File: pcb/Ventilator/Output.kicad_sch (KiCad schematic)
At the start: 16 parts, among them J3 Screw_Terminal_01x08, K1 FINDER-40.52.7.012.0000, K2 FINDER-40.52.7.012.0000, K3 FINDER-40.52.7.012.0000, Q1 NUD3160, Q2 NUD3160, Q3 NUD3160

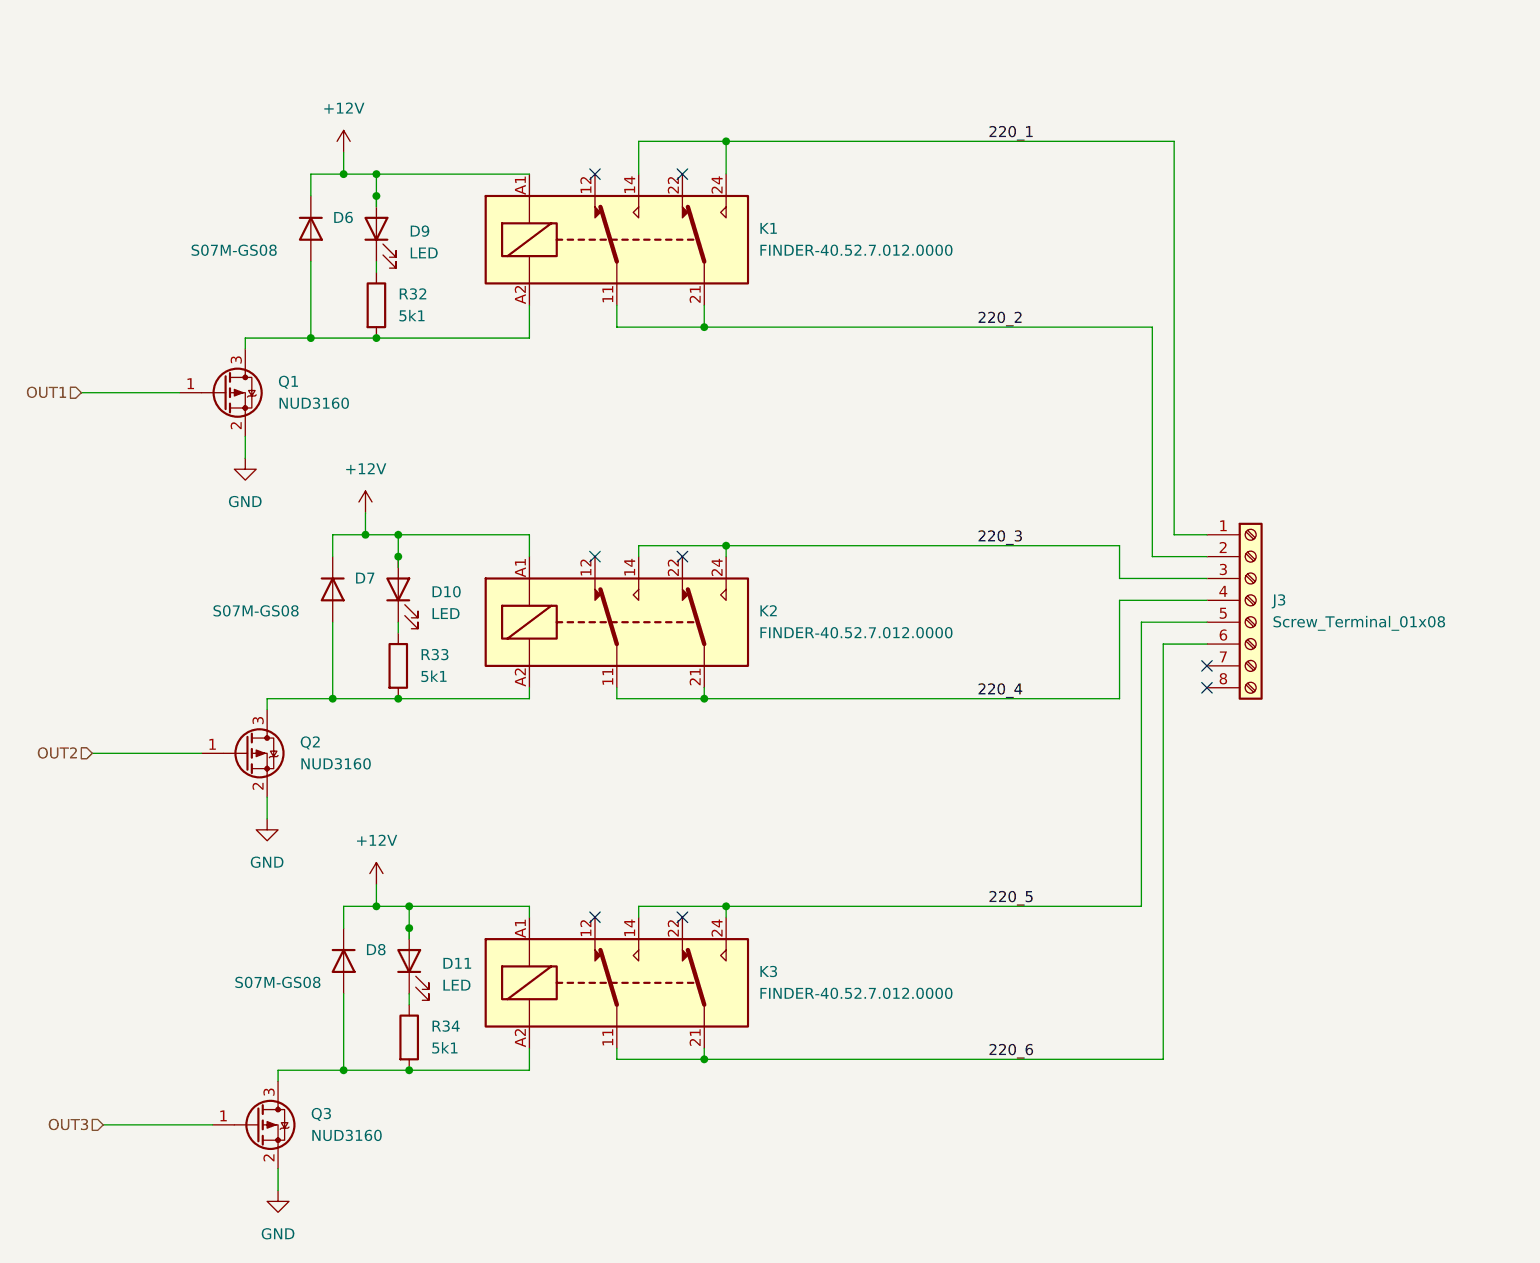
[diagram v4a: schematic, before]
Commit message: -Ventcontrol 1.2 (routed)
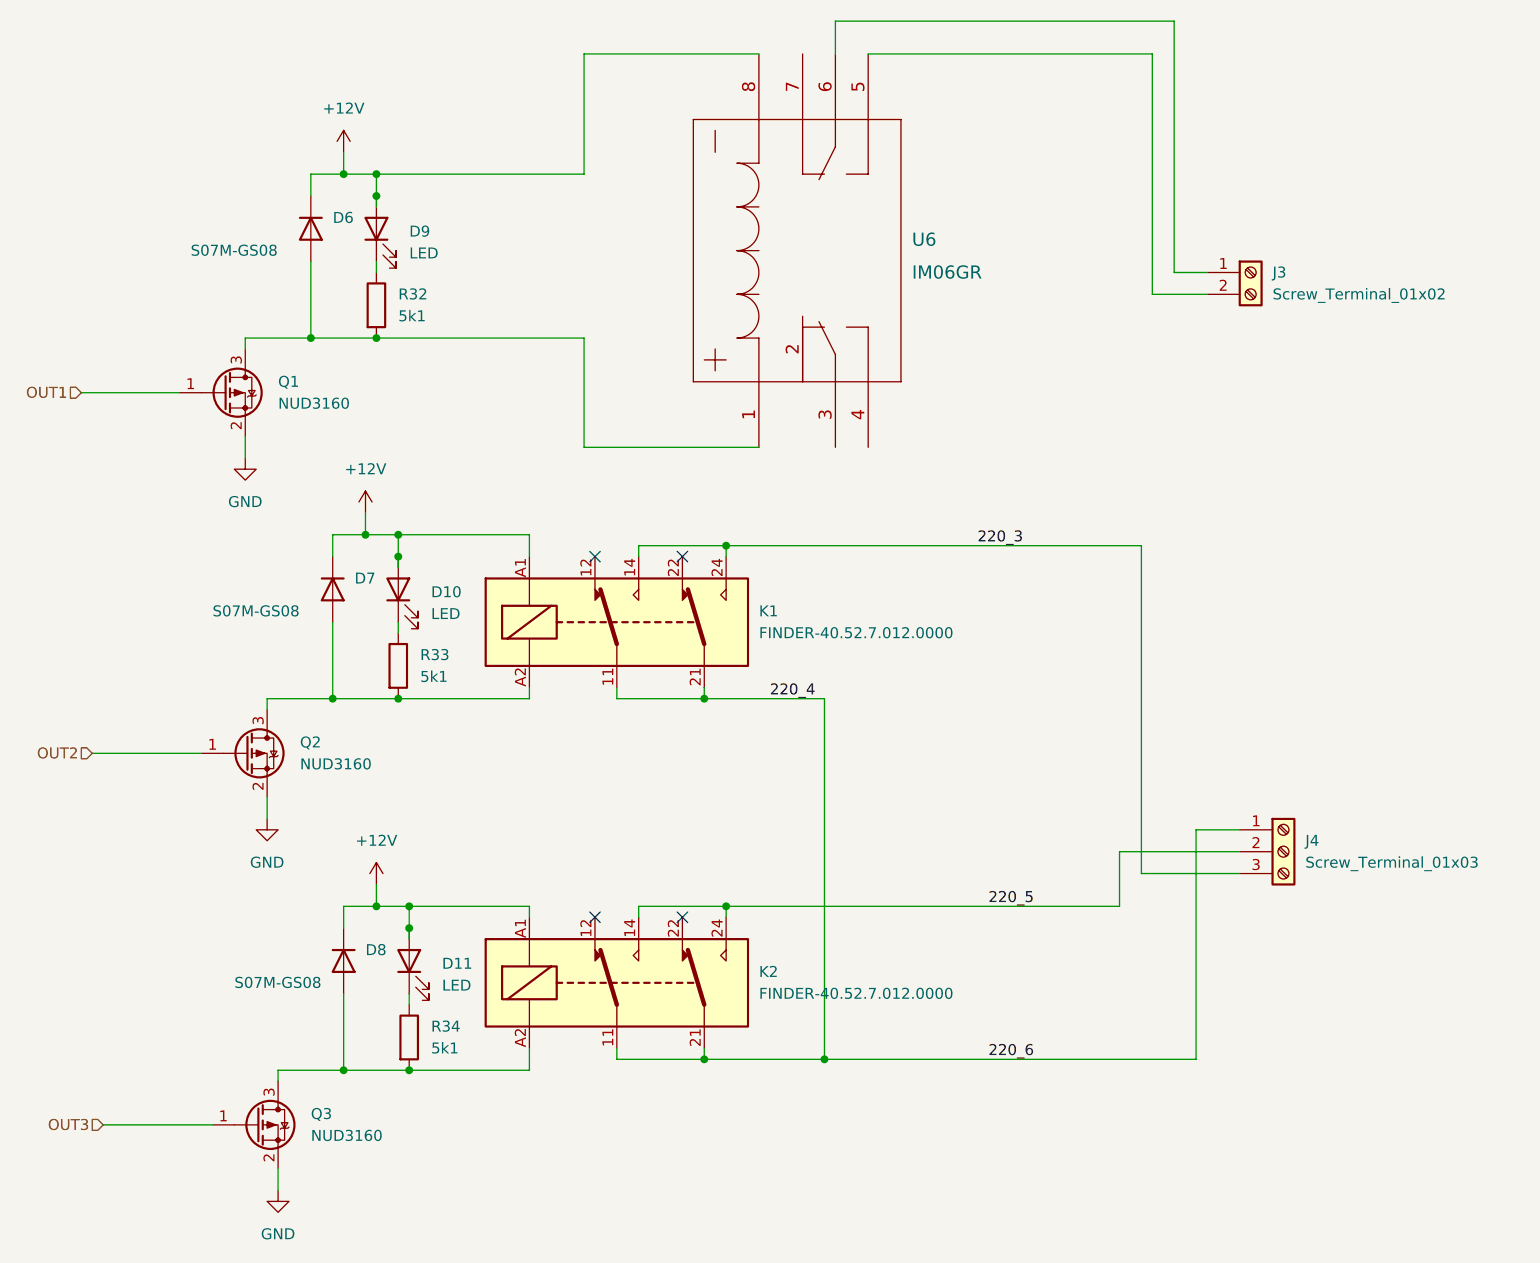
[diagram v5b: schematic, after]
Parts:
- removed J3: Screw_Terminal_01x08, TerminalBlock_Phoenix:TerminalBlock_Phoenix_MKDS-1,5-8_1x08_P5.00mm_Horizontal, symbol Connector:Screw_Terminal_01x08
- removed K1: FINDER-40.52.7.012.0000, Relay_THT:Relay_DPDT_Finder_40.52, symbol Relay:FINDER-40.52
- added J3: Screw_Terminal_01x02, TerminalBlock_Phoenix:TerminalBlock_Phoenix_MKDS-1,5-2-5.08_1x02_P5.08mm_Horizontal, symbol Connector:Screw_Terminal_01x02
- added J4: Screw_Terminal_01x03, TerminalBlock_Phoenix:TerminalBlock_Phoenix_MKDS-1,5-3-5.08_1x03_P5.08mm_Horizontal, symbol Connector:Screw_Terminal_01x03
- added U6: IM06GR, IM06GR:IM06GR, symbol 2023-01-29_17-38-59:IM06GR
- renumbered K2 to K1, K3 to K2
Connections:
- net 220_6 is gone; now on net 220_4: K2.11, K2.21
- net +12V: now also U6.8
- net 220_3: now also J4.3 (Pin_3)
- net 220_4: now also J4.1 (Pin_1)
- net 220_5: now also J4.2 (Pin_2)
- net at D6.2 (A), Q1.3 (D), R32.2: now also U6.1
- new net: J3.2 (Pin_2), U6.5
- new net: J3.1 (Pin_1), U6.6
- no-connect marks 8 -> 4

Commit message: - last changes
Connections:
- no-connect marks 4 -> 8
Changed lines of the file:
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@@
   )
   (no_connect (at 146.05 85.09))
+  (no_connect (at 160.02 57.15))
   (no_connect (at 146.05 127))
   (no_connect (at 135.89 85.09))
+  (no_connect (at 160.02 26.67))
+  (no_connect (at 163.83 72.39))
+  (no_connect (at 167.64 72.39))
   (no_connect (at 135.89 127))
   (wire (pts (xy 163.83 22.86) (xy 203.2 22.86))

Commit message: - as ordered
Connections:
- net +12V: now also U6.1; no longer U6.8
- net at D6.2 (A), Q1.3 (D), R32.2: now also U6.8; no longer U6.1
- net at U6.3: now also J3.1 (Pin_1), U6.6
- net at U6.4: now also J3.2 (Pin_2), U6.5
- no-connect marks 8 -> 5
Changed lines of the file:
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@@
   (junction (at 151.13 125.73) (diameter 0) (color 0 0 0 0)
   )
+  (junction (at 189.23 22.86) (diameter 0) (color 0 0 0 0)
+  )
   (junction (at 114.3 128.27) (diameter 0) (color 0 0 0 0)
   )
@@
   (junction (at 148.59 143.51) (diameter 0) (color 0 0 0 0)
   )
+  (junction (at 184.15 26.67) (diameter 0) (color 0 0 0 0)
+  )
   (junction (at 113.03 82.55) (diameter 0) (color 0 0 0 0)
   )
@@
   )
   (no_connect (at 146.05 85.09))
-  (no_connect (at 160.02 57.15))
   (no_connect (at 146.05 127))
   (no_connect (at 135.89 85.09))
-  (no_connect (at 160.02 26.67))
-  (no_connect (at 163.83 72.39))
-  (no_connect (at 167.64 72.39))
+  (no_connect (at 160.02 72.39))
   (no_connect (at 135.89 127))
-  (wire (pts (xy 163.83 22.86) (xy 203.2 22.86))
+  (wire (pts (xy 163.83 22.86) (xy 189.23 22.86))
     (stroke (width 0) (type default) (color 0 0 0 0))
   )
@@
     (stroke (width 0) (type default) (color 0 0 0 0))
   )
+  (wire (pts (xy 189.23 22.86) (xy 203.2 22.86))
+    (stroke (width 0) (type default) (color 0 0 0 0))
+  )
   (wire (pts (xy 199.39 121.92) (xy 210.82 121.92))
     (stroke (width 0) (type default) (color 0 0 0 0))
   )
-  (wire (pts (xy 134.62 26.67) (xy 154.94 26.67))
-    (stroke (width 0) (type default) (color 0 0 0 0))
-  )
   (wire (pts (xy 128.27 144.78) (xy 128.27 142.24))
     (stroke (width 0) (type default) (color 0 0 0 0))
   )
-  (wire (pts (xy 110.49 59.69) (xy 134.62 59.69))
+  (wire (pts (xy 110.49 59.69) (xy 137.16 59.69))
     (stroke (width 0) (type default) (color 0 0 0 0))
   )
@@
     (stroke (width 0) (type default) (color 0 0 0 0))
   )
-  (wire (pts (xy 110.49 40.64) (xy 134.62 40.64))
+  (wire (pts (xy 110.49 40.64) (xy 138.43 40.64))
     (stroke (width 0) (type default) (color 0 0 0 0))
   )
@@
     (stroke (width 0) (type default) (color 0 0 0 0))
   )
-  (wire (pts (xy 134.62 72.39) (xy 154.94 72.39))
-    (stroke (width 0) (type default) (color 0 0 0 0))
-  )
   (wire (pts (xy 110.49 43.18) (xy 110.49 44.45))
     (stroke (width 0) (type default) (color 0 0 0 0))
   )
+  (wire (pts (xy 138.43 26.67) (xy 154.94 26.67))
+    (stroke (width 0) (type default) (color 0 0 0 0))
+  )
   (wire (pts (xy 105.41 85.09) (xy 105.41 82.55))
     (stroke (width 0) (type default) (color 0 0 0 0))
@@
     (stroke (width 0) (type default) (color 0 0 0 0))
   )
+  (wire (pts (xy 184.15 26.67) (xy 184.15 74.93))
+    (stroke (width 0) (type default) (color 0 0 0 0))
+  )
   (wire (pts (xy 162.56 101.6) (xy 162.56 143.51))
     (stroke (width 0) (type default) (color 0 0 0 0))
@@
     (stroke (width 0) (type default) (color 0 0 0 0))
   )
+  (wire (pts (xy 137.16 59.69) (xy 137.16 72.39))
+    (stroke (width 0) (type default) (color 0 0 0 0))
+  )
   (wire (pts (xy 110.49 40.64) (xy 110.49 43.18))
     (stroke (width 0) (type default) (color 0 0 0 0))
@@
     (stroke (width 0) (type default) (color 0 0 0 0))
   )
+  (wire (pts (xy 167.64 74.93) (xy 167.64 72.39))
+    (stroke (width 0) (type default) (color 0 0 0 0))
+  )
   (wire (pts (xy 128.27 101.6) (xy 128.27 100.33))
     (stroke (width 0) (type default) (color 0 0 0 0))
@@
     (stroke (width 0) (type default) (color 0 0 0 0))
   )
+  (wire (pts (xy 138.43 40.64) (xy 138.43 26.67))
+    (stroke (width 0) (type default) (color 0 0 0 0))
+  )
+  (wire (pts (xy 167.64 26.67) (xy 184.15 26.67))
+    (stroke (width 0) (type default) (color 0 0 0 0))
+  )
   (wire (pts (xy 140.97 127) (xy 140.97 125.73))
     (stroke (width 0) (type default) (color 0 0 0 0))
@@
     (stroke (width 0) (type default) (color 0 0 0 0))
   )
-  (wire (pts (xy 134.62 40.64) (xy 134.62 26.67))
-    (stroke (width 0) (type default) (color 0 0 0 0))
-  )
   (wire (pts (xy 114.3 128.27) (xy 114.3 129.54))
     (stroke (width 0) (type default) (color 0 0 0 0))
   )
+  (wire (pts (xy 137.16 72.39) (xy 154.94 72.39))
+    (stroke (width 0) (type default) (color 0 0 0 0))
+  )
   (wire (pts (xy 148.59 100.33) (xy 148.59 101.6))
     (stroke (width 0) (type default) (color 0 0 0 0))
@@
     (stroke (width 0) (type default) (color 0 0 0 0))
   )
+  (wire (pts (xy 184.15 26.67) (xy 200.66 26.67))
+    (stroke (width 0) (type default) (color 0 0 0 0))
+  )
   (wire (pts (xy 102.87 50.8) (xy 102.87 59.69))
     (stroke (width 0) (type default) (color 0 0 0 0))
@@
     (stroke (width 0) (type default) (color 0 0 0 0))
   )
-  (wire (pts (xy 134.62 59.69) (xy 134.62 72.39))
-    (stroke (width 0) (type default) (color 0 0 0 0))
-  )
   (wire (pts (xy 128.27 125.73) (xy 128.27 127))
     (stroke (width 0) (type default) (color 0 0 0 0))
@@
     (stroke (width 0) (type default) (color 0 0 0 0))
   )
-  (wire (pts (xy 167.64 26.67) (xy 200.66 26.67))
-    (stroke (width 0) (type default) (color 0 0 0 0))
-  )
   (wire (pts (xy 151.13 83.82) (xy 151.13 85.09))
     (stroke (width 0) (type default) (color 0 0 0 0))
@@
     (stroke (width 0) (type default) (color 0 0 0 0))
   )
+  (wire (pts (xy 163.83 78.74) (xy 163.83 72.39))
+    (stroke (width 0) (type default) (color 0 0 0 0))
+  )
   (wire (pts (xy 113.03 82.55) (xy 128.27 82.55))
     (stroke (width 0) (type default) (color 0 0 0 0))
@@
   )
   (wire (pts (xy 114.3 125.73) (xy 114.3 128.27))
+    (stroke (width 0) (type default) (color 0 0 0 0))
+  )
+  (wire (pts (xy 189.23 22.86) (xy 189.23 78.74))
+    (stroke (width 0) (type default) (color 0 0 0 0))
+  )
+  (wire (pts (xy 184.15 74.93) (xy 167.64 74.93))
+    (stroke (width 0) (type default) (color 0 0 0 0))
+  )
+  (wire (pts (xy 189.23 78.74) (xy 163.83 78.74))
     (stroke (width 0) (type default) (color 0 0 0 0))
   )
@@
     (pin "2")
   )
-  (symbol (lib_id "2023-01-29_17-38-59:IM06GR") (at 154.94 72.39 90) (unit 1)
+  (symbol (lib_id "2023-01-29_17-38-59:IM06GR") (at 154.94 26.67 90) (mirror x) (unit 1)
     (in_bom yes) (on_board yes) (fields_autoplaced)
     (property "Reference" "U6" (id 0) (at 172.72 48.26 90)
@@
       (effects (font (size 1.524 1.524)) hide)
     )
-    (property "Datasheet" "" (id 3) (at 154.94 72.39 0)
+    (property "Datasheet" "" (id 3) (at 154.94 26.67 0)
       (effects (font (size 1.524 1.524)))
     )
